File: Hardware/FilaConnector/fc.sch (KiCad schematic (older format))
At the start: 5 parts, among them J1 Conn_1, J2 Conn_2, J3 PWR_IN, SW1 PowerSel

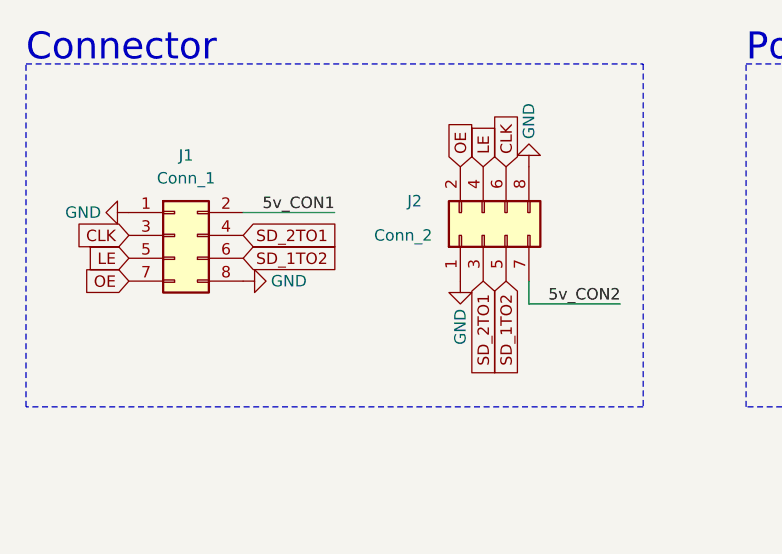
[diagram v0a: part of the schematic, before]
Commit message: updated wall cell and connector
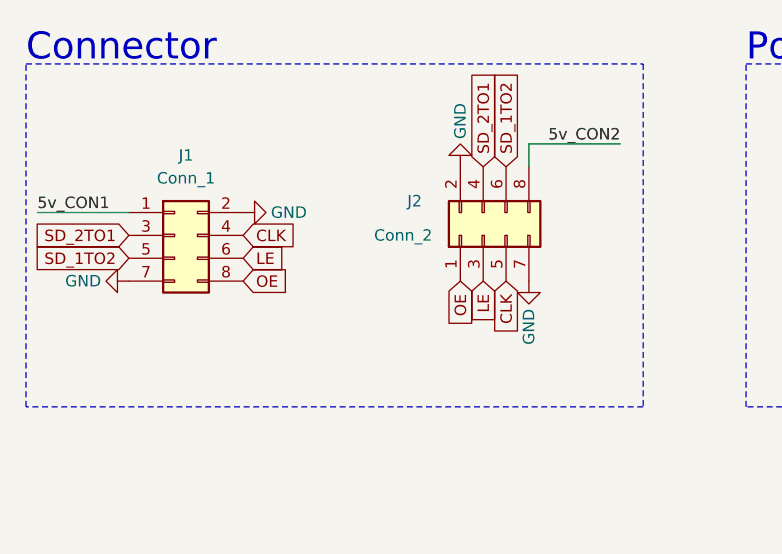
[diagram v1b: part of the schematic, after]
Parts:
- H1: footprint MountingHole:MountingHole_3.2mm_M3_Pad_Via -> MountingHole:MountingHole_2.2mm_M2_Pad
- J1, J2: footprint Connector_PinSocket_2.54mm:PinSocket_2x04_P2.54mm_Vertical -> Connector_PinHeader_2.54mm:PinHeader_2x04_P2.54mm_Vertical
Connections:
- net 5v_CON1: now also J1.1 (Pin_1); no longer J1.2 (Pin_2)
- net 5v_CON2: now also J2.8 (Pin_8); no longer J2.7 (Pin_7)
- net CLK: now also J1.4 (Pin_4), J2.5 (Pin_5); no longer J1.3 (Pin_3), J2.6 (Pin_6)
- net GND: now also J1.2 (Pin_2), J1.7 (Pin_7), J2.2 (Pin_2), J2.7 (Pin_7); no longer J1.1 (Pin_1), J1.8 (Pin_8), J2.1 (Pin_1), J2.8 (Pin_8)
- net LE: now also J1.6 (Pin_6), J2.3 (Pin_3); no longer J1.5 (Pin_5), J2.4 (Pin_4)
- net OE: now also J1.8 (Pin_8), J2.1 (Pin_1); no longer J1.7 (Pin_7), J2.2 (Pin_2)
- net SD_1TO2: now also J1.5 (Pin_5), J2.6 (Pin_6); no longer J1.6 (Pin_6), J2.5 (Pin_5)
- net SD_2TO1: now also J1.3 (Pin_3), J2.4 (Pin_4); no longer J1.4 (Pin_4), J2.3 (Pin_3)
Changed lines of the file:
@@
 F 0 "J2" V 4150 2700 50  0000 C CNN
 F 1 "Conn_2" V 4000 2750 50  0000 C CNN
-F 2 "Connector_PinSocket_2.54mm:PinSocket_2x04_P2.54mm_Vertical" H 4000 2400 50  0001 C CNN
+F 2 "Connector_PinHeader_2.54mm:PinHeader_2x04_P2.54mm_Vertical" H 4000 2400 50  0001 C CNN
 F 3 "~" H 4000 2400 50  0001 C CNN
 	1    4000 2400
 	0    -1   -1   0
 $EndComp
+Text GLabel 2450 2500 0    50   Input ~ 0
+SD_1TO2
+Text GLabel 4100 2100 1    50   Input ~ 0
+SD_1TO2
 Text GLabel 2950 2500 2    50   Input ~ 0
-SD_1TO2
+LE
+Text GLabel 2950 2600 2    50   Input ~ 0
+OE
 Text GLabel 4100 2600 3    50   Input ~ 0
-SD_1TO2
-Text GLabel 2450 2500 0    50   Input ~ 0
+CLK
+Text GLabel 4000 2600 3    50   Input ~ 0
 LE
-Text GLabel 2450 2600 0    50   Input ~ 0
+Text GLabel 3900 2600 3    50   Input ~ 0
 OE
-Text GLabel 4100 2100 1    50   Input ~ 0
-CLK
-Text GLabel 4000 2100 1    50   Input ~ 0
-LE
-Text GLabel 3900 2100 1    50   Input ~ 0
-OE
-Text GLabel 2450 2400 0    50   Input ~ 0
+Text GLabel 2950 2400 2    50   Input ~ 0
 CLK
 Text Label 5500 2350 0    50   ~ 0
@@
 Text Label 7100 2450 2    50   ~ 0
 5v_CON2
-Text Label 3350 2300 2    50   ~ 0
+Text Label 2050 2300 0    50   ~ 0
 5v_CON1
-Text Label 4600 2700 2    50   ~ 0
+Text Label 4600 2000 2    50   ~ 0
 5v_CON2
 Wire Wire Line
-	2950 2300 3350 2300
+	2450 2300 2050 2300
 Wire Wire Line
 	7100 2350 6700 2350
@@
 L power:GND #PWR0101
 U 1 1 6069982E
-P 3900 2600
-F 0 "#PWR0101" H 3900 2350 50  0001 C CNN
-F 1 "GND" V 3900 2400 50  0000 C CNN
-F 2 "" H 3900 2600 50  0001 C CNN
-F 3 "" H 3900 2600 50  0001 C CNN
-	1    3900 2600
-	1    0    0    -1
+P 3900 2100
+F 0 "#PWR0101" H 3900 1850 50  0001 C CNN
+F 1 "GND" V 3900 1900 50  0000 C CNN
+F 2 "" H 3900 2100 50  0001 C CNN
+F 3 "" H 3900 2100 50  0001 C CNN
+	1    3900 2100
+	1    0    0    1
 $EndComp
 $Comp
 L power:GND #PWR0102
 U 1 1 6067B802
-P 2950 2600
-F 0 "#PWR0102" H 2950 2350 50  0001 C CNN
-F 1 "GND" V 2950 2400 50  0000 C CNN
-F 2 "" H 2950 2600 50  0001 C CNN
-F 3 "" H 2950 2600 50  0001 C CNN
-	1    2950 2600
-	0    -1   -1   0
+P 2450 2600
+F 0 "#PWR0102" H 2450 2350 50  0001 C CNN
+F 1 "GND" V 2450 2400 50  0000 C CNN
+F 2 "" H 2450 2600 50  0001 C CNN
+F 3 "" H 2450 2600 50  0001 C CNN
+	1    2450 2600
+	0    1    -1   0
 $EndComp
 $Comp
 L power:GND #PWR0103
 U 1 1 6068ACBF
-P 2450 2300
-F 0 "#PWR0103" H 2450 2050 50  0001 C CNN
-F 1 "GND" V 2450 2100 50  0000 C CNN
-F 2 "" H 2450 2300 50  0001 C CNN
-F 3 "" H 2450 2300 50  0001 C CNN
-	1    2450 2300
-	0    1    1    0
+P 2950 2300
+F 0 "#PWR0103" H 2950 2050 50  0001 C CNN
+F 1 "GND" V 2950 2100 50  0000 C CNN
+F 2 "" H 2950 2300 50  0001 C CNN
+F 3 "" H 2950 2300 50  0001 C CNN
+	1    2950 2300
+	0    -1   1    0
 $EndComp
 $Comp
 L power:GND #PWR0104
 U 1 1 6067A66E
-P 4200 2100
-F 0 "#PWR0104" H 4200 1850 50  0001 C CNN
-F 1 "GND" V 4200 1900 50  0000 C CNN
-F 2 "" H 4200 2100 50  0001 C CNN
-F 3 "" H 4200 2100 50  0001 C CNN
-	1    4200 2100
-	-1   0    0    1
+P 4200 2600
+F 0 "#PWR0104" H 4200 2350 50  0001 C CNN
+F 1 "GND" V 4200 2400 50  0000 C CNN
+F 2 "" H 4200 2600 50  0001 C CNN
+F 3 "" H 4200 2600 50  0001 C CNN
+	1    4200 2600
+	-1   0    0    -1
 $EndComp
 $Comp
@@
 F 0 "J1" H 2700 2750 50  0000 C CNN
 F 1 "Conn_1" H 2700 2650 50  0000 C CNN
-F 2 "Connector_PinSocket_2.54mm:PinSocket_2x04_P2.54mm_Vertical" H 2650 2400 50  0001 C CNN
+F 2 "Connector_PinHeader_2.54mm:PinHeader_2x04_P2.54mm_Vertical" H 2650 2400 50  0001 C CNN
 F 3 "~" H 2650 2400 50  0001 C CNN
 	1    2650 2400
 	1    0    0    -1
 $EndComp
-Text GLabel 2950 2400 2    50   Input ~ 0
+Text GLabel 2450 2400 0    50   Input ~ 0
 SD_2TO1
-Text GLabel 4000 2600 3    50   Input ~ 0
+Text GLabel 4000 2100 1    50   Input ~ 0
 SD_2TO1
 Wire Notes Line
@@
 F 0 "H1" V 8604 2300 50  0000 L CNN
 F 1 "MountingHole_Pad" V 8695 2300 50  0000 L CNN
-F 2 "MountingHole:MountingHole_3.2mm_M3_Pad_Via" H 8650 2150 50  0001 C CNN
+F 2 "MountingHole:MountingHole_2.2mm_M2_Pad" H 8650 2150 50  0001 C CNN
 F 3 "~" H 8650 2150 50  0001 C CNN
 	1    8650 2150
@@
 	8850 3550 8950 3550
 Wire Wire Line
-	4200 2600 4200 2700
-Wire Wire Line
-	4200 2700 4600 2700
+	4200 2100 4200 2000
+Wire Wire Line
+	4200 2000 4600 2000
 Wire Notes Line
 	7900 3050 9700 3050

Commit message: merged all
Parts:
- added H1: MountingHole_Pad, MountingHole:MountingHole_3.2mm_M3_Pad, symbol Mechanical:MountingHole_Pad
- H2: renamed from H1; footprint MountingHole:MountingHole_2.2mm_M2_Pad -> MountingHole:MountingHole_3.2mm_M3_Pad
- J1, J2: footprint Connector_PinHeader_2.54mm:PinHeader_2x04_P2.54mm_Vertical -> Connector_PinSocket_2.54mm:PinSocket_2x04_P2.54mm_Vertical
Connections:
- net 5v_CON1: now also J1.2 (Pin_2); no longer J1.1 (Pin_1)
- net 5v_CON2: now also J2.7 (Pin_7); no longer J2.8 (Pin_8)
- net CLK: now also J1.3 (Pin_3), J2.6 (Pin_6); no longer J1.4 (Pin_4), J2.5 (Pin_5)
- net GND: now also J1.1 (Pin_1), J1.8 (Pin_8), J2.1 (Pin_1), J2.8 (Pin_8), H1.1; no longer J1.2 (Pin_2), J1.7 (Pin_7), J2.2 (Pin_2), J2.7 (Pin_7)
- net LE: now also J1.5 (Pin_5), J2.4 (Pin_4); no longer J1.6 (Pin_6), J2.3 (Pin_3)
- net OE: now also J1.7 (Pin_7), J2.2 (Pin_2); no longer J1.8 (Pin_8), J2.1 (Pin_1)
- net SD_1TO2: now also J1.6 (Pin_6), J2.5 (Pin_5); no longer J1.5 (Pin_5), J2.6 (Pin_6)
- net SD_2TO1: now also J1.4 (Pin_4), J2.3 (Pin_3); no longer J1.3 (Pin_3), J2.4 (Pin_4)
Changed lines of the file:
@@
 F 0 "J2" V 4150 2700 50  0000 C CNN
 F 1 "Conn_2" V 4000 2750 50  0000 C CNN
-F 2 "Connector_PinHeader_2.54mm:PinHeader_2x04_P2.54mm_Vertical" H 4000 2400 50  0001 C CNN
+F 2 "Connector_PinSocket_2.54mm:PinSocket_2x04_P2.54mm_Vertical" H 4000 2400 50  0001 C CNN
 F 3 "~" H 4000 2400 50  0001 C CNN
 	1    4000 2400
 	0    -1   -1   0
 $EndComp
+Text GLabel 2950 2500 2    50   Input ~ 0
+SD_1TO2
 Text GLabel 2450 2500 0    50   Input ~ 0
-SD_1TO2
+LE
+Text GLabel 2450 2600 0    50   Input ~ 0
+OE
 Text GLabel 4100 2100 1    50   Input ~ 0
-SD_1TO2
-Text GLabel 2950 2500 2    50   Input ~ 0
+CLK
+Text GLabel 4000 2100 1    50   Input ~ 0
 LE
-Text GLabel 2950 2600 2    50   Input ~ 0
+Text GLabel 3900 2100 1    50   Input ~ 0
 OE
-Text GLabel 4100 2600 3    50   Input ~ 0
-CLK
-Text GLabel 4000 2600 3    50   Input ~ 0
-LE
-Text GLabel 3900 2600 3    50   Input ~ 0
-OE
-Text GLabel 2950 2400 2    50   Input ~ 0
+Text GLabel 2450 2400 0    50   Input ~ 0
 CLK
 Text Label 5500 2350 0    50   ~ 0
@@
 Text Label 7100 2450 2    50   ~ 0
 5v_CON2
-Text Label 2050 2300 0    50   ~ 0
+Text Label 3350 2300 2    50   ~ 0
 5v_CON1
-Text Label 4600 2000 2    50   ~ 0
-5v_CON2
-Wire Wire Line
-	2450 2300 2050 2300
+Wire Wire Line
+	2950 2300 3350 2300
 Wire Wire Line
 	7100 2350 6700 2350
 Wire Wire Line
 	6700 2450 7100 2450
-$Comp
-L power:GND #PWR0101
-U 1 1 6069982E
-P 3900 2100
-F 0 "#PWR0101" H 3900 1850 50  0001 C CNN
-F 1 "GND" V 3900 1900 50  0000 C CNN
-F 2 "" H 3900 2100 50  0001 C CNN
-F 3 "" H 3900 2100 50  0001 C CNN
-	1    3900 2100
-	1    0    0    1
-$EndComp
 $Comp
 L power:GND #PWR0102
 U 1 1 6067B802
-P 2450 2600
-F 0 "#PWR0102" H 2450 2350 50  0001 C CNN
-F 1 "GND" V 2450 2400 50  0000 C CNN
-F 2 "" H 2450 2600 50  0001 C CNN
-F 3 "" H 2450 2600 50  0001 C CNN
-	1    2450 2600
-	0    1    -1   0
+P 2950 2600
+F 0 "#PWR0102" H 2950 2350 50  0001 C CNN
+F 1 "GND" V 2950 2400 50  0000 C CNN
+F 2 "" H 2950 2600 50  0001 C CNN
+F 3 "" H 2950 2600 50  0001 C CNN
+	1    2950 2600
+	0    -1   -1   0
 $EndComp
 $Comp
 L power:GND #PWR0103
 U 1 1 6068ACBF
-P 2950 2300
-F 0 "#PWR0103" H 2950 2050 50  0001 C CNN
-F 1 "GND" V 2950 2100 50  0000 C CNN
-F 2 "" H 2950 2300 50  0001 C CNN
-F 3 "" H 2950 2300 50  0001 C CNN
-	1    2950 2300
-	0    -1   1    0
+P 2450 2300
+F 0 "#PWR0103" H 2450 2050 50  0001 C CNN
+F 1 "GND" V 2450 2100 50  0000 C CNN
+F 2 "" H 2450 2300 50  0001 C CNN
+F 3 "" H 2450 2300 50  0001 C CNN
+	1    2450 2300
+	0    1    1    0
 $EndComp
 $Comp
 L power:GND #PWR0104
 U 1 1 6067A66E
-P 4200 2600
-F 0 "#PWR0104" H 4200 2350 50  0001 C CNN
-F 1 "GND" V 4200 2400 50  0000 C CNN
-F 2 "" H 4200 2600 50  0001 C CNN
-F 3 "" H 4200 2600 50  0001 C CNN
-	1    4200 2600
-	-1   0    0    -1
+P 4200 2100
+F 0 "#PWR0104" H 4200 1850 50  0001 C CNN
+F 1 "GND" V 4200 1900 50  0000 C CNN
+F 2 "" H 4200 2100 50  0001 C CNN
+F 3 "" H 4200 2100 50  0001 C CNN
+	1    4200 2100
+	-1   0    0    1
 $EndComp
 $Comp
@@
 F 0 "J1" H 2700 2750 50  0000 C CNN
 F 1 "Conn_1" H 2700 2650 50  0000 C CNN
-F 2 "Connector_PinHeader_2.54mm:PinHeader_2x04_P2.54mm_Vertical" H 2650 2400 50  0001 C CNN
+F 2 "Connector_PinSocket_2.54mm:PinSocket_2x04_P2.54mm_Vertical" H 2650 2400 50  0001 C CNN
 F 3 "~" H 2650 2400 50  0001 C CNN
 	1    2650 2400
 	1    0    0    -1
 $EndComp
-Text GLabel 2450 2400 0    50   Input ~ 0
-SD_2TO1
-Text GLabel 4000 2100 1    50   Input ~ 0
+Text GLabel 2950 2400 2    50   Input ~ 0
 SD_2TO1
 Wire Notes Line
@@
 Wire Notes Line
 	7450 3150 5150 3150
-Wire Notes Line
-	5150 3150 5150 1650
 Text Notes 5150 1650 0    118  ~ 0
 Power Selector
-$Comp
-L Mechanical:MountingHole_Pad H1
-U 1 1 606C30C3
-P 8650 2150
-F 0 "H1" V 8604 2300 50  0000 L CNN
-F 1 "MountingHole_Pad" V 8695 2300 50  0000 L CNN
-F 2 "MountingHole:MountingHole_2.2mm_M2_Pad" H 8650 2150 50  0001 C CNN
-F 3 "~" H 8650 2150 50  0001 C CNN
-	1    8650 2150
-	0    1    1    0
-$EndComp
 Wire Notes Line
 	7900 1650 9700 1650
@@
 Wire Notes Line
 	7900 2750 7900 1650
-$Comp
-L power:GND #PWR0105
-U 1 1 606C3F9B
-P 8450 2250
-F 0 "#PWR0105" H 8450 2000 50  0001 C CNN
-F 1 "GND" H 8455 2077 50  0000 C CNN
-F 2 "" H 8450 2250 50  0001 C CNN
-F 3 "" H 8450 2250 50  0001 C CNN
-	1    8450 2250
-	1    0    0    -1
-$EndComp
-Wire Wire Line
-	8550 2150 8450 2150
-Wire Wire Line
-	8450 2150 8450 2250
 Text Notes 7900 1650 0    118  ~ 0
 Mounting Hole
-Wire Notes Line
-	4700 1650 4700 3150
 Wire Notes Line
 	4700 3150 2000 3150
@@
 Wire Wire Line
 	8850 3550 8950 3550
-Wire Wire Line
-	4200 2100 4200 2000
-Wire Wire Line
-	4200 2000 4600 2000
 Wire Notes Line
 	7900 3050 9700 3050
@@
 Text Notes 7900 3050 0    118  ~ 0
 Power Input
+Wire Wire Line
+	4200 2700 4600 2700
+Wire Wire Line
+	4200 2600 4200 2700
+Wire Notes Line
+	4700 1650 4700 3150
+Wire Notes Line
+	5150 3150 5150 1650
+Text GLabel 4000 2600 3    50   Input ~ 0
+SD_2TO1
+$Comp
+L power:GND #PWR0101
+U 1 1 6069982E
+P 3900 2600
+F 0 "#PWR0101" H 3900 2350 50  0001 C CNN
+F 1 "GND" V 3900 2400 50  0000 C CNN
+F 2 "" H 3900 2600 50  0001 C CNN
+F 3 "" H 3900 2600 50  0001 C CNN
+	1    3900 2600
+	1    0    0    -1
+$EndComp
+Text Label 4600 2700 2    50   ~ 0
+5v_CON2
+Text GLabel 4100 2600 3    50   Input ~ 0
+SD_1TO2
+Connection ~ 8450 2150
+Wire Wire Line
+	8450 1900 8550 1900
+Wire Wire Line
+	8450 2150 8450 1900
+$Comp
+L Mechanical:MountingHole_Pad H1
+U 1 1 60760819
+P 8650 1900
+F 0 "H1" V 8604 2050 50  0000 L CNN
+F 1 "MountingHole_Pad" V 8695 2050 50  0000 L CNN
+F 2 "MountingHole:MountingHole_3.2mm_M3_Pad" H 8650 1900 50  0001 C CNN
+F 3 "~" H 8650 1900 50  0001 C CNN
+	1    8650 1900
+	0    1    1    0
+$EndComp
+Wire Wire Line
+	8450 2150 8450 2250
+Wire Wire Line
+	8550 2150 8450 2150
+$Comp
+L power:GND #PWR0105
+U 1 1 606C3F9B
+P 8450 2250
+F 0 "#PWR0105" H 8450 2000 50  0001 C CNN
+F 1 "GND" H 8455 2077 50  0000 C CNN
+F 2 "" H 8450 2250 50  0001 C CNN
+F 3 "" H 8450 2250 50  0001 C CNN
+	1    8450 2250
+	1    0    0    -1
+$EndComp
+$Comp
+L Mechanical:MountingHole_Pad H2
+U 1 1 606C30C3
+P 8650 2150
+F 0 "H2" V 8604 2300 50  0000 L CNN
+F 1 "MountingHole_Pad" V 8695 2300 50  0000 L CNN
+F 2 "MountingHole:MountingHole_3.2mm_M3_Pad" H 8650 2150 50  0001 C CNN
+F 3 "~" H 8650 2150 50  0001 C CNN
+	1    8650 2150
+	0    1    1    0
+$EndComp
 $EndSCHEMATC
